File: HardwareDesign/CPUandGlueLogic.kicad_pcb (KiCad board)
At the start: 2 copper layers, 35 parts, among them J001 Conn_02x40_Odd_Even, J100 Conn_01x02, U101 74HCT245, U102 74HCT245, U103 74HCT245, U104 74HCT365, U105 MAX708, U106 HD6809, U107 74HCT00, U108 74HCT27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

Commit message: restarted using JLCPCB template
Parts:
- moved C107 35.3 mm to (184.5, 126.5)
- moved C110 35.3 mm to (171.4, 147.8)
- moved C111 35.3 mm to (191.0, 126.5)
- moved C114 35.3 mm to (197.1, 121.1)
- moved J100 35.3 mm to (194.6, 110.1)
- moved U107 35.3 mm to (149.3, 129.4)
- moved C103 35.3 mm to (184.5, 122.5)
- moved C106 35.3 mm to (191.0, 122.5)
- moved R101 35.3 mm to (182.6, 118.9)
- moved R102 35.3 mm to (182.6, 115.7)
- moved U101 35.3 mm to (148.0, 102.3)
- moved U102 35.3 mm to (136.2, 102.3)
- moved U104 35.3 mm to (171.5, 102.3)
- moved U105 35.3 mm to (172.8, 124.4)
- moved U108 35.3 mm to (161.0, 124.4)
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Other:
- copper layers 2 -> 4
- net class Default: clearance 0.2 -> 0.127; trace_width 0.25 -> 0.127; via_dia 0.8 -> 0.6; via_drill 0.4 -> 0.3
- rule trace_clearance: 0.2 -> 0.127
- rule trace_min: 0.2 -> 0.127
- rule via_min_size: 0.4 -> 0.6

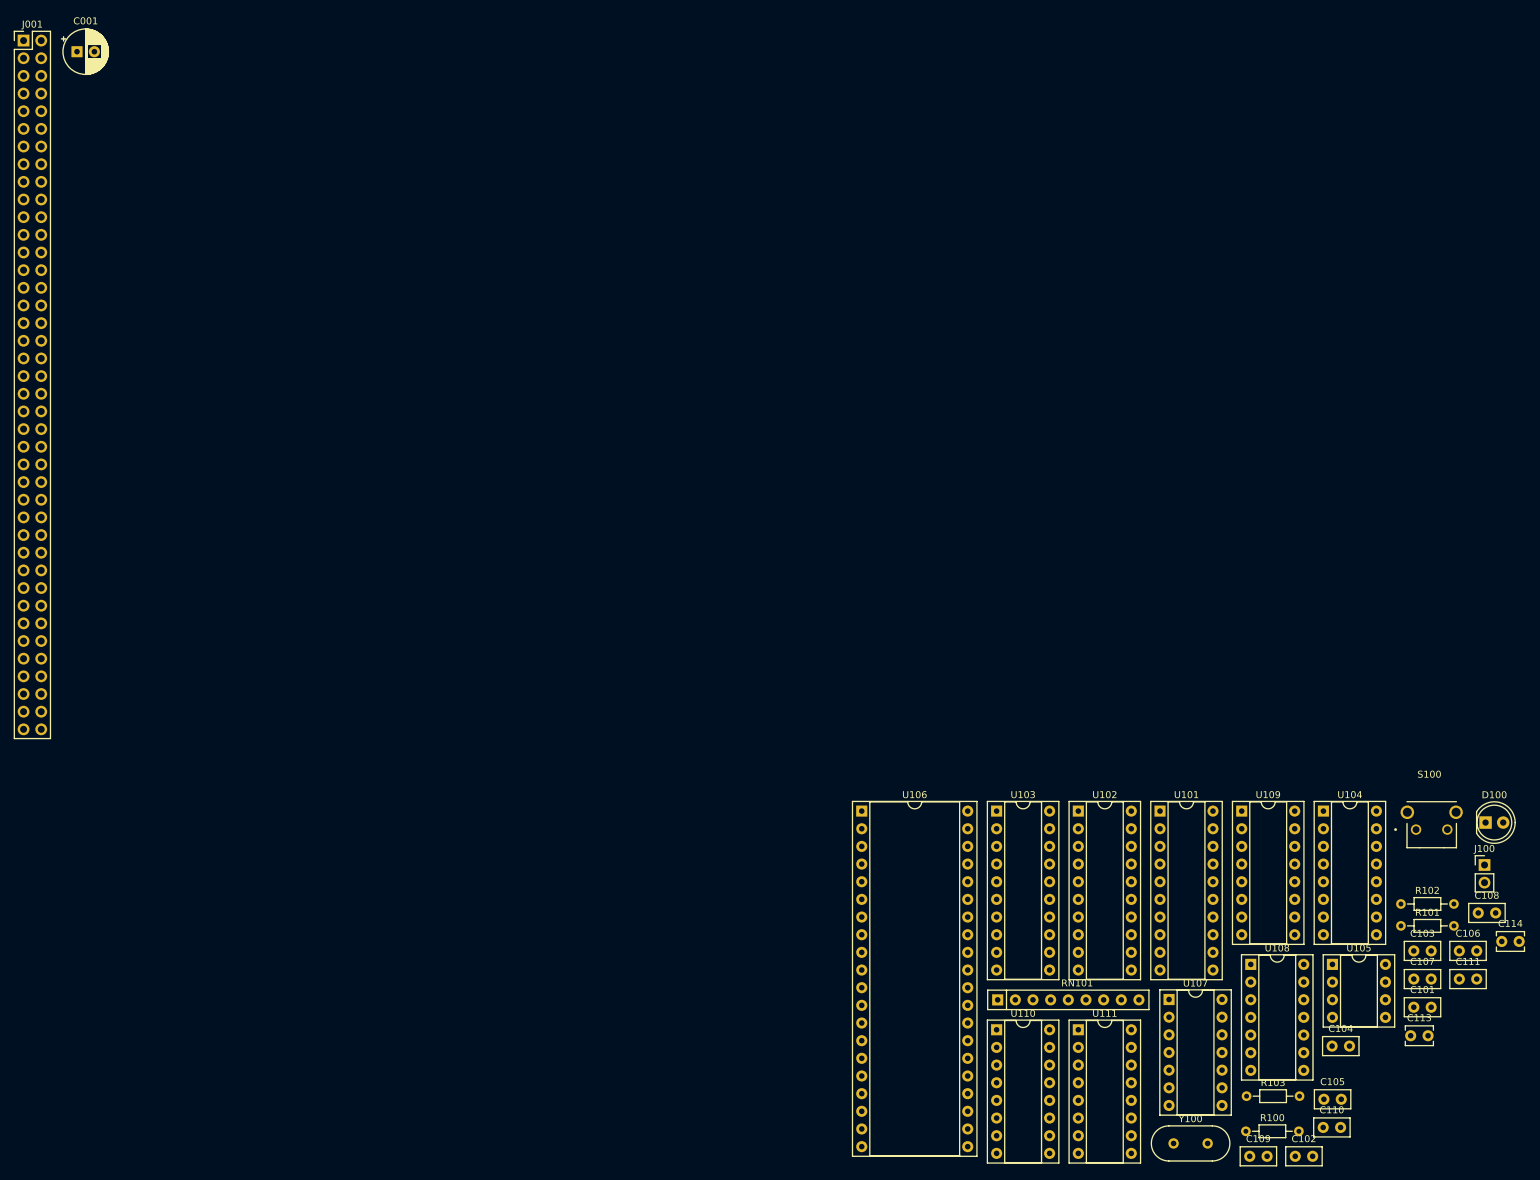
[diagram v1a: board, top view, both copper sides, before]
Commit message: components placed, started to route power rails
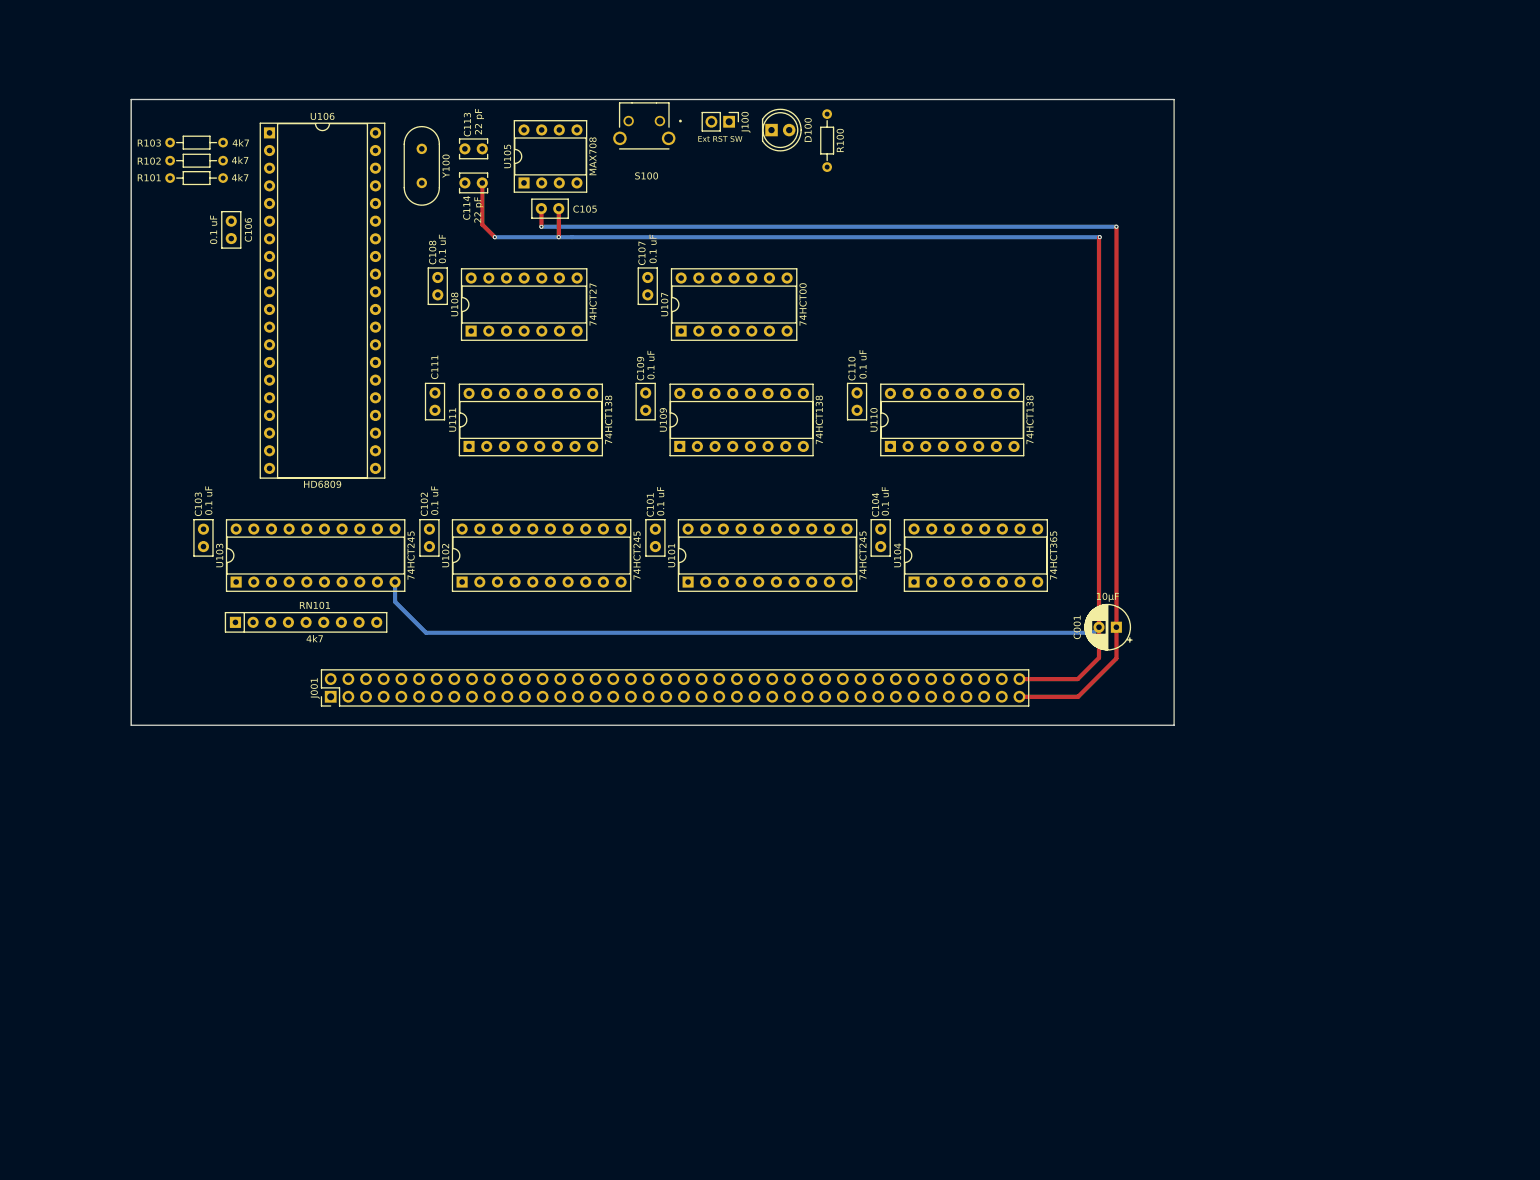
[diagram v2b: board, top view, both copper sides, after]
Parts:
- moved R101 207.1 mm to (5.60, 11.3)
- moved R103 206.8 mm to (5.60, 6.20)
- moved R102 206.8 mm to (5.60, 8.80)
- moved C106 205.5 mm to (14.4, 17.5), turned to 270 degrees
- moved C113 184.7 mm to (50.5, 7.10), turned to 180 degrees
- moved C103 184.3 mm to (10.4, 61.8), turned to 270 degrees
- moved C114 182.8 mm to (50.5, 12.0), turned to 180 degrees
- moved Y100 179.3 mm to (41.8, 7.10), turned to 270 degrees
- moved C108 175.3 mm to (44.1, 25.6), turned to 270 degrees
- moved C001 170.9 mm to (141.7, 75.9), turned to 180 degrees
- moved C105 170.5 mm to (59.0, 15.7)
- moved C111 169.7 mm to (43.7, 42.2), turned to 270 degrees
- moved U105 161.7 mm to (56.5, 12.0), turned to 90 degrees
- moved R100 158.2 mm to (100.1, 2.10), turned to 270 degrees
- moved C102 153.8 mm to (42.9, 61.8), turned to 270 degrees
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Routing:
- net GND: track 0.00 -> 279.2 mm, vias 0 -> 3
- net VCC: track 0.00 -> 163.6 mm, vias 0 -> 2
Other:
- board outline added: 150 x 90 mm
- copper layers 4 -> 2
- board text added: "Ext RST SW"

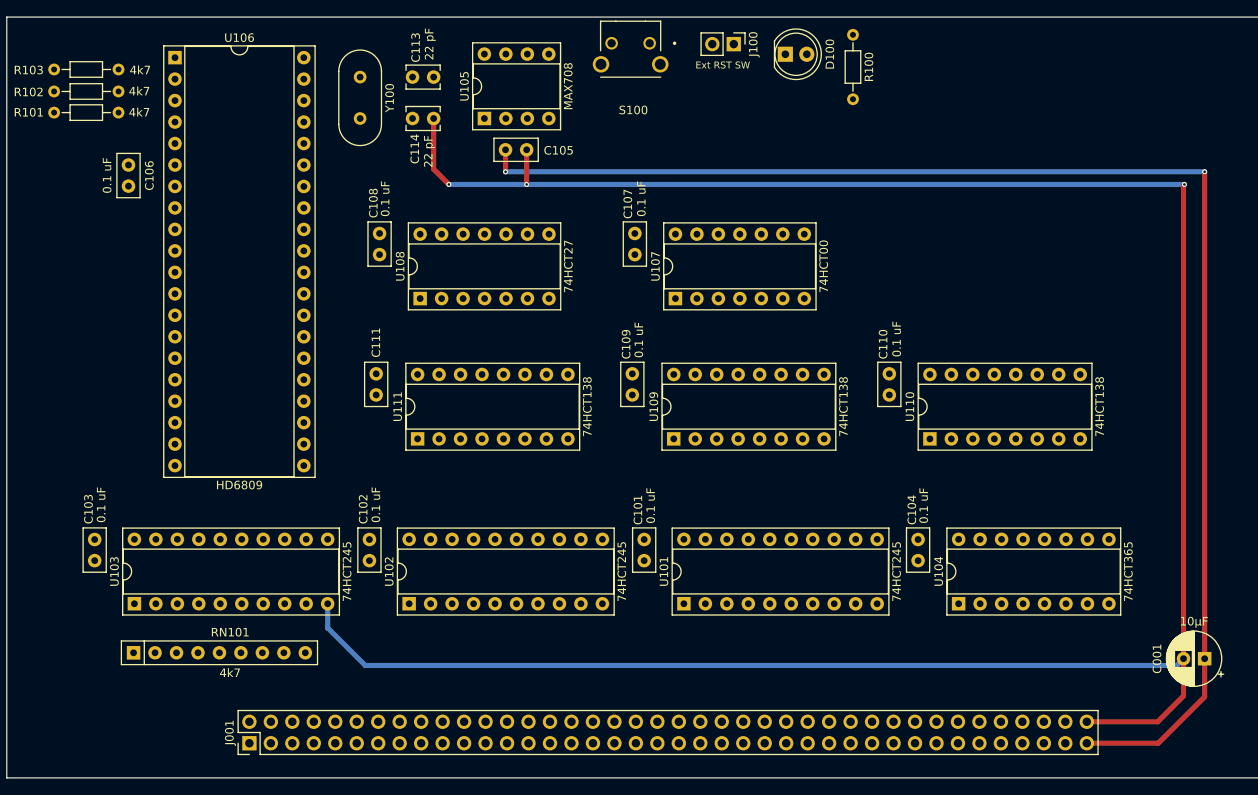
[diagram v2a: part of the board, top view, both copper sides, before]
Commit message: better placement of backplane connector, more routing
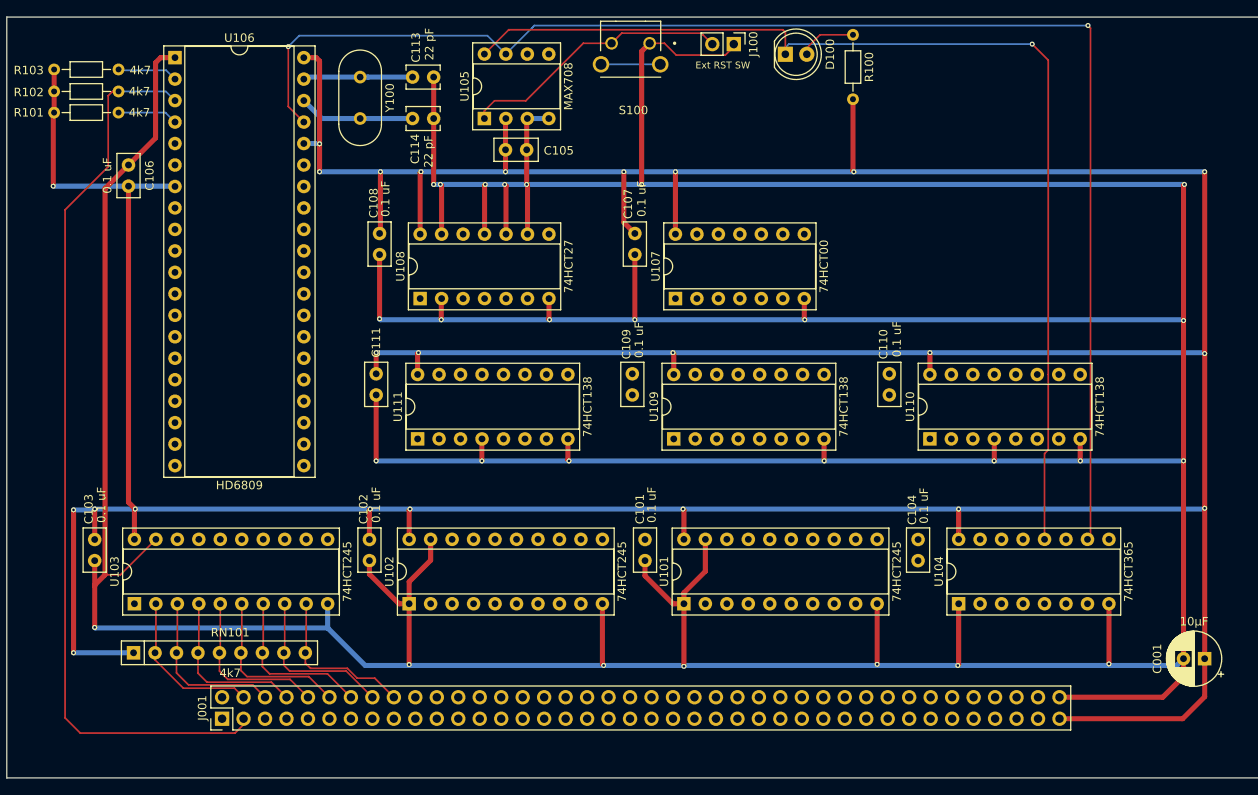
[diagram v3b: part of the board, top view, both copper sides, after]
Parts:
- moved J001 4.34 mm to (25.5, 83.0)
- moved C101 2.50 mm to (75.5, 61.8), turned to 270 degrees
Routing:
- net GND: track 279.2 -> 765.7 mm, vias 3 -> 27
- net VCC: track 163.6 -> 601.7 mm, vias 2 -> 24
- net /CPUandGlueLogic/Unbuf_~RST~: track 0.00 -> 168.2 mm, vias 0 -> 2
- net /CPUandGlueLogic/Unbuf_RST: track 0.00 -> 129.3 mm, vias 0 -> 1
- net /~IRQ: track 0.00 -> 107.2 mm
- net Net-(J100-Pad2): track 0.00 -> 32.2 mm
- net /D2: track 0.00 -> 19.9 mm
- net /D1: track 0.00 -> 19.9 mm
- net /D3: track 0.00 -> 19.8 mm
- net /D4: track 0.00 -> 19.7 mm
- net /D5: track 0.00 -> 19.5 mm
- net /D6: track 0.00 -> 19.4 mm
- net /D7: track 0.00 -> 19.2 mm
- net /D0: track 0.00 -> 19.0 mm
- net Net-(C114-Pad2): track 0.00 -> 13.7 mm
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
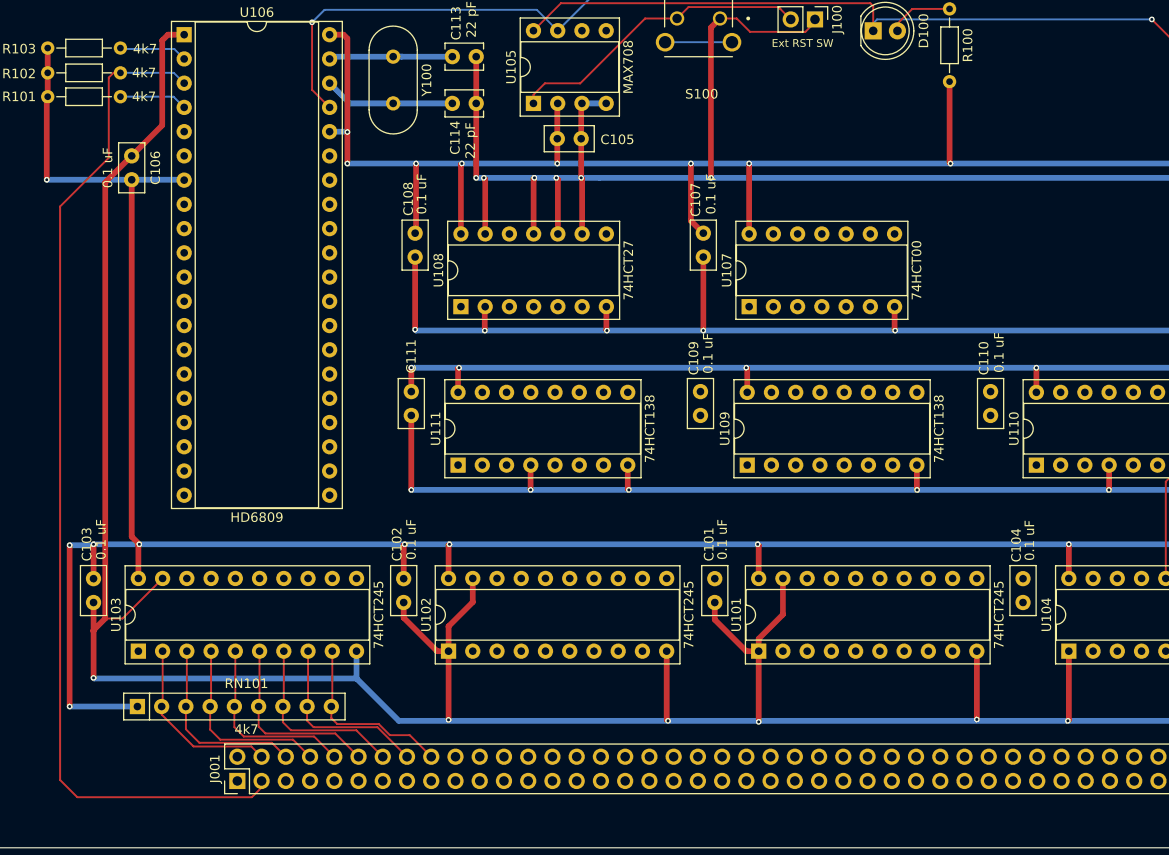
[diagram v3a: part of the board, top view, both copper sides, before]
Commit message: more signal routing
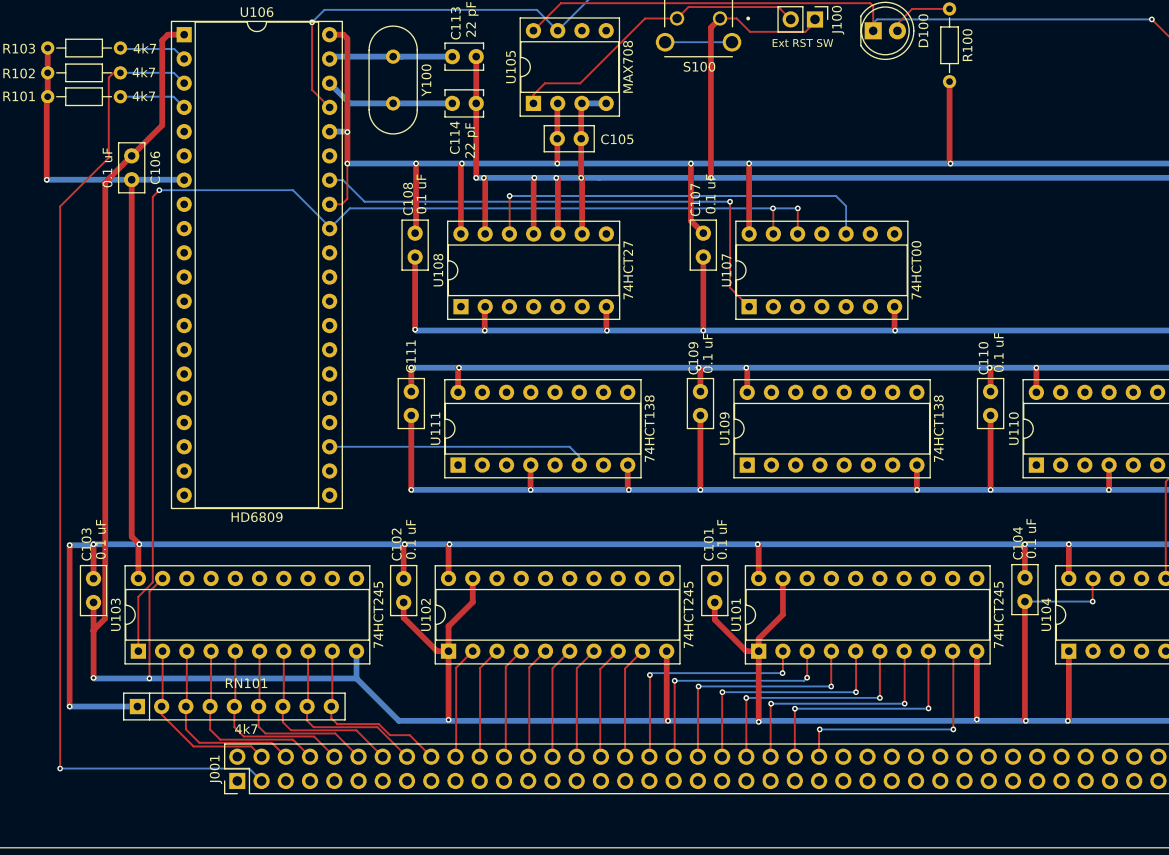
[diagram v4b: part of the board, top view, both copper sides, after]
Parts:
- moved C104 2.61 mm to (108.0, 61.7), turned to 270 degrees
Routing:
- net /CPUandGlueLogic/Unbuf_R~W~: track 0.00 -> 124.1 mm, vias 0 -> 3
- net /CPUandGlueLogic/Unbuf_E: track 0.00 -> 54.7 mm, vias 0 -> 1
- net Net-(U107-Pad10): track 0.00 -> 42.6 mm, vias 0 -> 1
- net GND: track 765.7 -> 806.6 mm, vias 27 -> 32
- net /CPUandGlueLogic/Unbuf_A15: track 0.00 -> 27.5 mm
- net /A7: track 0.00 -> 25.1 mm, vias 0 -> 2
- net /A5: track 0.00 -> 25.1 mm, vias 0 -> 2
- net /A3: track 0.00 -> 25.1 mm, vias 0 -> 2
- net /A4: track 0.00 -> 25.1 mm, vias 0 -> 2
- net /A6: track 0.00 -> 25.1 mm, vias 0 -> 2
- net /A2: track 0.00 -> 25.0 mm, vias 0 -> 2
- net /A0: track 0.00 -> 24.9 mm, vias 0 -> 2
- net /A1: track 0.00 -> 24.8 mm, vias 0 -> 2
- net VCC: track 601.7 -> 616.1 mm, vias 24 -> 27
- net /A14: track 0.00 -> 11.9 mm
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
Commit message: more signal routing, getting there...
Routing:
- net /CPUandGlueLogic/Unbuf_A8: track 0.00 -> 142.7 mm, vias 0 -> 3
- net /CPUandGlueLogic/Unbuf_A0: track 0.00 -> 100.8 mm, vias 0 -> 1
- net /CPUandGlueLogic/Unbuf_~WMEM~: track 0.00 -> 81.2 mm, vias 0 -> 1
- net /~ROMEN~: track 0.00 -> 70.8 mm, vias 0 -> 3
- net /CPUandGlueLogic/Unbuf_~RMEM~: track 0.00 -> 65.2 mm, vias 0 -> 1
- net /CPUandGlueLogic/Unbuf_E: track 54.7 -> 117.8 mm, vias 1 -> 2
- net /CPUandGlueLogic/Unbuf_A13: track 0.00 -> 59.2 mm, vias 0 -> 1
- net /CPUandGlueLogic/Unbuf_R~W~: track 124.1 -> 182.6 mm, vias 3 -> 4
- net /CPUandGlueLogic/Unbuf_D0: track 0.00 -> 54.7 mm, vias 0 -> 1
- net /CPUandGlueLogic/Unbuf_D1: track 0.00 -> 52.5 mm, vias 0 -> 1
- net /CPUandGlueLogic/Unbuf_A12: track 0.00 -> 51.8 mm, vias 0 -> 2
- net /CPUandGlueLogic/Unbuf_A14: track 0.00 -> 50.0 mm, vias 0 -> 2
- net /CPUandGlueLogic/Unbuf_A11: track 0.00 -> 49.8 mm
- net /CPUandGlueLogic/Unbuf_A10: track 0.00 -> 48.1 mm
- net /~IODEV13: track 0.00 -> 48.0 mm, vias 0 -> 1
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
